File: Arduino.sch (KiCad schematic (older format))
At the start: 20 parts

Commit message: Arduino layout
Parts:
- added R13, R14, R55: R, symbol R
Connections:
- net GND: now also R14.2, R55.2
- net at ARD1.1 (5V): now also R13.1
- net at ARD1.2 (GND): now also R14.1
- net at ARD1.3 (GND): now also R55.1
- new net +5V: R13.2
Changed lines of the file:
@@
 	7900 5200 7900 5600
 $Comp
-L GND #PWR67
+L GND #PWR057
 U 1 1 52FC2D3A
 P 7900 5600
-F 0 "#PWR67" H 7900 5600 30  0001 C CNN
+F 0 "#PWR057" H 7900 5600 30  0001 C CNN
 F 1 "GND" H 7900 5530 30  0001 C CNN
 F 2 "" H 7900 5600 60  0000 C CNN
@@
 $EndComp
 Wire Wire Line
-	2700 4000 2300 4000
+	2700 4000 2000 4000
 Wire Wire Line
 	3200 4000 3750 4000
 $Comp
-L +12P #PWR66
+L +12P #PWR058
 U 1 1 52FC23FA
-P 2300 3800
-F 0 "#PWR66" H 2300 3770 30  0001 C CNN
-F 1 "+12P" H 2300 3900 30  0000 C CNN
-F 2 "" H 2300 3800 60  0000 C CNN
-F 3 "" H 2300 3800 60  0000 C CNN
-	1    2300 3800
+P 2000 3800
+F 0 "#PWR058" H 2000 3770 30  0001 C CNN
+F 1 "+12P" H 2000 3900 30  0000 C CNN
+F 2 "" H 2000 3800 60  0000 C CNN
+F 3 "" H 2000 3800 60  0000 C CNN
+	1    2000 3800
 	1    0    0    -1
 $EndComp
 Wire Wire Line
-	2300 4000 2300 3800
+	2000 4000 2000 3800
 Text HLabel 7100 4400 2    60   Output ~ 0
 ~RESET
@@
 Wire Wire Line
 	5650 5000 6200 5000
+$Comp
+L R R13
+U 1 1 531F5FF6
+P 2950 3400
+F 0 "R13" V 3030 3400 40  0000 C CNN
+F 1 "R" V 2957 3401 40  0000 C CNN
+F 2 "" V 2880 3400 30  0000 C CNN
+F 3 "" H 2950 3400 30  0000 C CNN
+	1    2950 3400
+	0    1    -1   0
+$EndComp
+Wire Wire Line
+	2700 3400 2000 3400
+Wire Wire Line
+	3200 3400 3750 3400
+Wire Wire Line
+	2000 3400 2000 3200
+$Comp
+L +5V #PWR059
+U 1 1 531F6007
+P 2000 3200
+F 0 "#PWR059" H 2000 3290 20  0001 C CNN
+F 1 "+5V" H 2000 3290 30  0000 C CNN
+F 2 "" H 2000 3200 60  0000 C CNN
+F 3 "" H 2000 3200 60  0000 C CNN
+	1    2000 3200
+	1    0    0    -1
+$EndComp
+$Comp
+L R R14
+U 1 1 531F6023
+P 2950 3600
+F 0 "R14" V 3030 3600 40  0000 C CNN
+F 1 "R" V 2957 3601 40  0000 C CNN
+F 2 "" V 2880 3600 30  0000 C CNN
+F 3 "" H 2950 3600 30  0000 C CNN
+	1    2950 3600
+	0    1    -1   0
+$EndComp
+Wire Wire Line
+	3200 3600 3750 3600
+$Comp
+L R R55
+U 1 1 531F602A
+P 2950 3800
+F 0 "R55" V 3030 3800 40  0000 C CNN
+F 1 "R" V 2957 3801 40  0000 C CNN
+F 2 "" V 2880 3800 30  0000 C CNN
+F 3 "" H 2950 3800 30  0000 C CNN
+	1    2950 3800
+	0    1    -1   0
+$EndComp
+Wire Wire Line
+	3200 3800 3750 3800
+Wire Wire Line
+	2250 3600 2250 3800
+$Comp
+L GND #PWR060
+U 1 1 531F6032
+P 2250 3800
+F 0 "#PWR060" H 2250 3800 30  0001 C CNN
+F 1 "GND" H 2250 3730 30  0001 C CNN
+F 2 "" H 2250 3800 60  0000 C CNN
+F 3 "" H 2250 3800 60  0000 C CNN
+	1    2250 3800
+	1    0    0    -1
+$EndComp
+Wire Wire Line
+	2250 3600 2700 3600
+Wire Wire Line
+	2700 3800 2500 3800
+Wire Wire Line
+	2500 3800 2500 3600
+Connection ~ 2500 3600
 $EndSCHEMATC

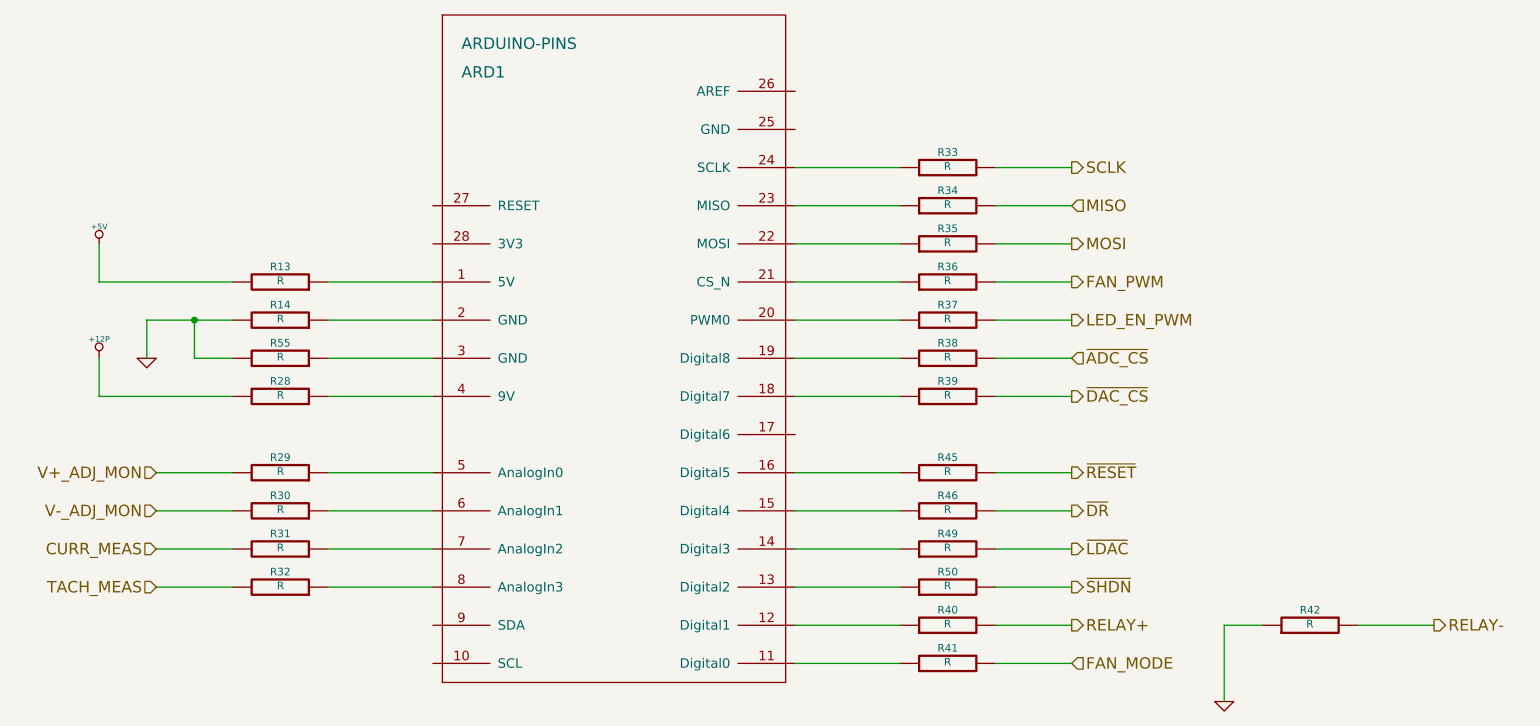
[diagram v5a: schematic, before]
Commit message: Assigned values to passives in Arduino, power adjustment monitor, relay and terminal block schematics
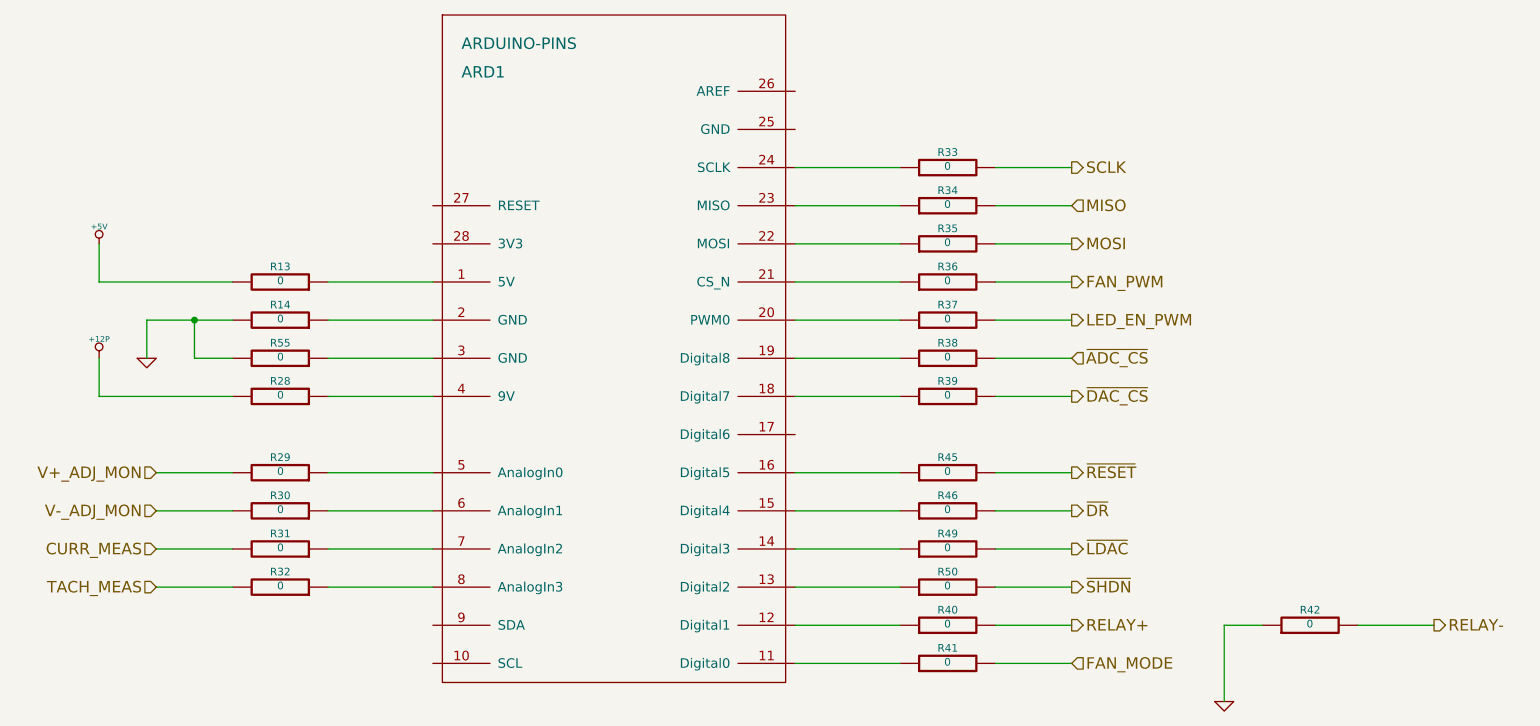
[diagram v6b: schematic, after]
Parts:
- R13, R14, R28, R29, R30, R31, R32, R33, R34, R35, R36, R37, R38, R39, R40, R41, R42, R45, R46, R49, R50, R55: value R -> 0
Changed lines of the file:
@@
 P 6450 3400
 F 0 "R36" V 6530 3400 40  0000 C CNN
-F 1 "R" V 6457 3401 40  0000 C CNN
+F 1 "0" V 6457 3401 40  0000 C CNN
 F 2 "" V 6380 3400 30  0000 C CNN
 F 3 "" H 6450 3400 30  0000 C CNN
@@
 P 6450 5200
 F 0 "R40" V 6530 5200 40  0000 C CNN
-F 1 "R" V 6457 5201 40  0000 C CNN
+F 1 "0" V 6457 5201 40  0000 C CNN
 F 2 "" V 6380 5200 30  0000 C CNN
 F 3 "" H 6450 5200 30  0000 C CNN
@@
 P 2950 5000
 F 0 "R32" V 3030 5000 40  0000 C CNN
-F 1 "R" V 2957 5001 40  0000 C CNN
+F 1 "0" V 2957 5001 40  0000 C CNN
 F 2 "" V 2880 5000 30  0000 C CNN
 F 3 "" H 2950 5000 30  0000 C CNN
@@
 P 2950 4800
 F 0 "R31" V 3030 4800 40  0000 C CNN
-F 1 "R" V 2957 4801 40  0000 C CNN
+F 1 "0" V 2957 4801 40  0000 C CNN
 F 2 "" V 2880 4800 30  0000 C CNN
 F 3 "" H 2950 4800 30  0000 C CNN
@@
 P 2950 4600
 F 0 "R30" V 3030 4600 40  0000 C CNN
-F 1 "R" V 2957 4601 40  0000 C CNN
+F 1 "0" V 2957 4601 40  0000 C CNN
 F 2 "" V 2880 4600 30  0000 C CNN
 F 3 "" H 2950 4600 30  0000 C CNN
@@
 P 2950 4400
 F 0 "R29" V 3030 4400 40  0000 C CNN
-F 1 "R" V 2957 4401 40  0000 C CNN
+F 1 "0" V 2957 4401 40  0000 C CNN
 F 2 "" V 2880 4400 30  0000 C CNN
 F 3 "" H 2950 4400 30  0000 C CNN
@@
 P 6450 3000
 F 0 "R34" V 6530 3000 40  0000 C CNN
-F 1 "R" V 6457 3001 40  0000 C CNN
+F 1 "0" V 6457 3001 40  0000 C CNN
 F 2 "" V 6380 3000 30  0000 C CNN
 F 3 "" H 6450 3000 30  0000 C CNN
@@
 P 6450 2800
 F 0 "R33" V 6530 2800 40  0000 C CNN
-F 1 "R" V 6457 2801 40  0000 C CNN
+F 1 "0" V 6457 2801 40  0000 C CNN
 F 2 "" V 6380 2800 30  0000 C CNN
 F 3 "" H 6450 2800 30  0000 C CNN
@@
 P 6450 4000
 F 0 "R39" V 6530 4000 40  0000 C CNN
-F 1 "R" V 6457 4001 40  0000 C CNN
+F 1 "0" V 6457 4001 40  0000 C CNN
 F 2 "" V 6380 4000 30  0000 C CNN
 F 3 "" H 6450 4000 30  0000 C CNN
@@
 P 6450 3200
 F 0 "R35" V 6530 3200 40  0000 C CNN
-F 1 "R" V 6457 3201 40  0000 C CNN
+F 1 "0" V 6457 3201 40  0000 C CNN
 F 2 "" V 6380 3200 30  0000 C CNN
 F 3 "" H 6450 3200 30  0000 C CNN
@@
 P 8350 5200
 F 0 "R42" V 8430 5200 40  0000 C CNN
-F 1 "R" V 8357 5201 40  0000 C CNN
+F 1 "0" V 8357 5201 40  0000 C CNN
 F 2 "" V 8280 5200 30  0000 C CNN
 F 3 "" H 8350 5200 30  0000 C CNN
@@
 P 6450 3600
 F 0 "R37" V 6530 3600 40  0000 C CNN
-F 1 "R" V 6457 3601 40  0000 C CNN
+F 1 "0" V 6457 3601 40  0000 C CNN
 F 2 "" V 6380 3600 30  0000 C CNN
 F 3 "" H 6450 3600 30  0000 C CNN
@@
 P 6450 3800
 F 0 "R38" V 6530 3800 40  0000 C CNN
-F 1 "R" V 6457 3801 40  0000 C CNN
+F 1 "0" V 6457 3801 40  0000 C CNN
 F 2 "" V 6380 3800 30  0000 C CNN
 F 3 "" H 6450 3800 30  0000 C CNN
@@
 P 6450 5400
 F 0 "R41" V 6530 5400 40  0000 C CNN
-F 1 "R" V 6457 5401 40  0000 C CNN
+F 1 "0" V 6457 5401 40  0000 C CNN
 F 2 "" V 6380 5400 30  0000 C CNN
 F 3 "" H 6450 5400 30  0000 C CNN
@@
 P 2950 4000
 F 0 "R28" V 3030 4000 40  0000 C CNN
-F 1 "R" V 2957 4001 40  0000 C CNN
+F 1 "0" V 2957 4001 40  0000 C CNN
 F 2 "" V 2880 4000 30  0000 C CNN
 F 3 "" H 2950 4000 30  0000 C CNN
@@
 P 6450 4400
 F 0 "R45" V 6530 4400 40  0000 C CNN
-F 1 "R" V 6457 4401 40  0000 C CNN
+F 1 "0" V 6457 4401 40  0000 C CNN
 F 2 "" V 6380 4400 30  0000 C CNN
 F 3 "" H 6450 4400 30  0000 C CNN
@@
 P 6450 4600
 F 0 "R46" V 6530 4600 40  0000 C CNN
-F 1 "R" V 6457 4601 40  0000 C CNN
+F 1 "0" V 6457 4601 40  0000 C CNN
 F 2 "" V 6380 4600 30  0000 C CNN
 F 3 "" H 6450 4600 30  0000 C CNN
@@
 P 6450 4800
 F 0 "R49" V 6530 4800 40  0000 C CNN
-F 1 "R" V 6457 4801 40  0000 C CNN
+F 1 "0" V 6457 4801 40  0000 C CNN
 F 2 "" V 6380 4800 30  0000 C CNN
 F 3 "" H 6450 4800 30  0000 C CNN
@@
 P 6450 5000
 F 0 "R50" V 6530 5000 40  0000 C CNN
-F 1 "R" V 6457 5001 40  0000 C CNN
+F 1 "0" V 6457 5001 40  0000 C CNN
 F 2 "" V 6380 5000 30  0000 C CNN
 F 3 "" H 6450 5000 30  0000 C CNN
@@
 P 2950 3400
 F 0 "R13" V 3030 3400 40  0000 C CNN
-F 1 "R" V 2957 3401 40  0000 C CNN
+F 1 "0" V 2957 3401 40  0000 C CNN
 F 2 "" V 2880 3400 30  0000 C CNN
 F 3 "" H 2950 3400 30  0000 C CNN
@@
 P 2950 3600
 F 0 "R14" V 3030 3600 40  0000 C CNN
-F 1 "R" V 2957 3601 40  0000 C CNN
+F 1 "0" V 2957 3601 40  0000 C CNN
 F 2 "" V 2880 3600 30  0000 C CNN
 F 3 "" H 2950 3600 30  0000 C CNN
@@
 P 2950 3800
 F 0 "R55" V 3030 3800 40  0000 C CNN
-F 1 "R" V 2957 3801 40  0000 C CNN
+F 1 "0" V 2957 3801 40  0000 C CNN
 F 2 "" V 2880 3800 30  0000 C CNN
 F 3 "" H 2950 3800 30  0000 C CNN

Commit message: Back-annotated footprints into the schematic
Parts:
- ARD1: footprint (none) -> BenchBudEE:Arduino
- R13, R14, R28, R29, R30, R31, R32, R33, R34, R35, R36, R37, R38, R39, R40, R41, R42, R45, R46, R49, R50, R55: footprint (none) -> BenchBudEE:Resistor_SMD0805_Blob
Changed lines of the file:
@@
 F 0 "ARD1" H 3900 5900 60  0000 L CNN
 F 1 "ARDUINO-PINS" H 3900 6050 60  0000 L CNN
-F 2 "" H 4700 4100 60  0000 C CNN
+F 2 "BenchBudEE:Arduino" H 4700 4100 60  0001 C CNN
 F 3 "" H 4700 4100 60  0000 C CNN
 	1    4700 4100
@@
 F 0 "R36" V 6530 3400 40  0000 C CNN
 F 1 "0" V 6457 3401 40  0000 C CNN
-F 2 "" V 6380 3400 30  0000 C CNN
+F 2 "BenchBudEE:Resistor_SMD0805_Blob" V 6380 3400 30  0001 C CNN
 F 3 "" H 6450 3400 30  0000 C CNN
 	1    6450 3400
@@
 F 0 "R40" V 6530 5200 40  0000 C CNN
 F 1 "0" V 6457 5201 40  0000 C CNN
-F 2 "" V 6380 5200 30  0000 C CNN
+F 2 "BenchBudEE:Resistor_SMD0805_Blob" V 6380 5200 30  0001 C CNN
 F 3 "" H 6450 5200 30  0000 C CNN
 	1    6450 5200
@@
 	7900 5200 7900 5600
 $Comp
-L GND #PWR061
+L GND #PWR060
 U 1 1 52FC2D3A
 P 7900 5600
-F 0 "#PWR061" H 7900 5600 30  0001 C CNN
+F 0 "#PWR060" H 7900 5600 30  0001 C CNN
 F 1 "GND" H 7900 5530 30  0001 C CNN
 F 2 "" H 7900 5600 60  0000 C CNN
@@
 F 0 "R32" V 3030 5000 40  0000 C CNN
 F 1 "0" V 2957 5001 40  0000 C CNN
-F 2 "" V 2880 5000 30  0000 C CNN
+F 2 "BenchBudEE:Resistor_SMD0805_Blob" V 2880 5000 30  0001 C CNN
 F 3 "" H 2950 5000 30  0000 C CNN
 	1    2950 5000
@@
 F 0 "R31" V 3030 4800 40  0000 C CNN
 F 1 "0" V 2957 4801 40  0000 C CNN
-F 2 "" V 2880 4800 30  0000 C CNN
+F 2 "BenchBudEE:Resistor_SMD0805_Blob" V 2880 4800 30  0001 C CNN
 F 3 "" H 2950 4800 30  0000 C CNN
 	1    2950 4800
@@
 F 0 "R30" V 3030 4600 40  0000 C CNN
 F 1 "0" V 2957 4601 40  0000 C CNN
-F 2 "" V 2880 4600 30  0000 C CNN
+F 2 "BenchBudEE:Resistor_SMD0805_Blob" V 2880 4600 30  0001 C CNN
 F 3 "" H 2950 4600 30  0000 C CNN
 	1    2950 4600
@@
 F 0 "R29" V 3030 4400 40  0000 C CNN
 F 1 "0" V 2957 4401 40  0000 C CNN
-F 2 "" V 2880 4400 30  0000 C CNN
+F 2 "BenchBudEE:Resistor_SMD0805_Blob" V 2880 4400 30  0001 C CNN
 F 3 "" H 2950 4400 30  0000 C CNN
 	1    2950 4400
@@
 F 0 "R34" V 6530 3000 40  0000 C CNN
 F 1 "0" V 6457 3001 40  0000 C CNN
-F 2 "" V 6380 3000 30  0000 C CNN
+F 2 "BenchBudEE:Resistor_SMD0805_Blob" V 6380 3000 30  0001 C CNN
 F 3 "" H 6450 3000 30  0000 C CNN
 	1    6450 3000
@@
 F 0 "R33" V 6530 2800 40  0000 C CNN
 F 1 "0" V 6457 2801 40  0000 C CNN
-F 2 "" V 6380 2800 30  0000 C CNN
+F 2 "BenchBudEE:Resistor_SMD0805_Blob" V 6380 2800 30  0001 C CNN
 F 3 "" H 6450 2800 30  0000 C CNN
 	1    6450 2800
@@
 F 0 "R39" V 6530 4000 40  0000 C CNN
 F 1 "0" V 6457 4001 40  0000 C CNN
-F 2 "" V 6380 4000 30  0000 C CNN
+F 2 "BenchBudEE:Resistor_SMD0805_Blob" V 6380 4000 30  0001 C CNN
 F 3 "" H 6450 4000 30  0000 C CNN
 	1    6450 4000
@@
 F 0 "R35" V 6530 3200 40  0000 C CNN
 F 1 "0" V 6457 3201 40  0000 C CNN
-F 2 "" V 6380 3200 30  0000 C CNN
+F 2 "BenchBudEE:Resistor_SMD0805_Blob" V 6380 3200 30  0001 C CNN
 F 3 "" H 6450 3200 30  0000 C CNN
 	1    6450 3200
@@
 F 0 "R42" V 8430 5200 40  0000 C CNN
 F 1 "0" V 8357 5201 40  0000 C CNN
-F 2 "" V 8280 5200 30  0000 C CNN
+F 2 "BenchBudEE:Resistor_SMD0805_Blob" V 8280 5200 30  0001 C CNN
 F 3 "" H 8350 5200 30  0000 C CNN
 	1    8350 5200
@@
 F 0 "R37" V 6530 3600 40  0000 C CNN
 F 1 "0" V 6457 3601 40  0000 C CNN
-F 2 "" V 6380 3600 30  0000 C CNN
+F 2 "BenchBudEE:Resistor_SMD0805_Blob" V 6380 3600 30  0001 C CNN
 F 3 "" H 6450 3600 30  0000 C CNN
 	1    6450 3600
@@
 F 0 "R38" V 6530 3800 40  0000 C CNN
 F 1 "0" V 6457 3801 40  0000 C CNN
-F 2 "" V 6380 3800 30  0000 C CNN
+F 2 "BenchBudEE:Resistor_SMD0805_Blob" V 6380 3800 30  0001 C CNN
 F 3 "" H 6450 3800 30  0000 C CNN
 	1    6450 3800
@@
 F 0 "R41" V 6530 5400 40  0000 C CNN
 F 1 "0" V 6457 5401 40  0000 C CNN
-F 2 "" V 6380 5400 30  0000 C CNN
+F 2 "BenchBudEE:Resistor_SMD0805_Blob" V 6380 5400 30  0001 C CNN
 F 3 "" H 6450 5400 30  0000 C CNN
 	1    6450 5400
@@
 F 0 "R28" V 3030 4000 40  0000 C CNN
 F 1 "0" V 2957 4001 40  0000 C CNN
-F 2 "" V 2880 4000 30  0000 C CNN
+F 2 "BenchBudEE:Resistor_SMD0805_Blob" V 2880 4000 30  0001 C CNN
 F 3 "" H 2950 4000 30  0000 C CNN
 	1    2950 4000
@@
 	3200 4000 3750 4000
 $Comp
-L +12P #PWR062
+L +12P #PWR061
 U 1 1 52FC23FA
 P 2000 3800
-F 0 "#PWR062" H 2000 3770 30  0001 C CNN
+F 0 "#PWR061" H 2000 3770 30  0001 C CNN
 F 1 "+12P" H 2000 3900 30  0000 C CNN
 F 2 "" H 2000 3800 60  0000 C CNN
@@
 F 0 "R45" V 6530 4400 40  0000 C CNN
 F 1 "0" V 6457 4401 40  0000 C CNN
-F 2 "" V 6380 4400 30  0000 C CNN
+F 2 "BenchBudEE:Resistor_SMD0805_Blob" V 6380 4400 30  0001 C CNN
 F 3 "" H 6450 4400 30  0000 C CNN
 	1    6450 4400
@@
 F 0 "R46" V 6530 4600 40  0000 C CNN
 F 1 "0" V 6457 4601 40  0000 C CNN
-F 2 "" V 6380 4600 30  0000 C CNN
+F 2 "BenchBudEE:Resistor_SMD0805_Blob" V 6380 4600 30  0001 C CNN
 F 3 "" H 6450 4600 30  0000 C CNN
 	1    6450 4600
@@
 F 0 "R49" V 6530 4800 40  0000 C CNN
 F 1 "0" V 6457 4801 40  0000 C CNN
-F 2 "" V 6380 4800 30  0000 C CNN
+F 2 "BenchBudEE:Resistor_SMD0805_Blob" V 6380 4800 30  0001 C CNN
 F 3 "" H 6450 4800 30  0000 C CNN
 	1    6450 4800
@@
 F 0 "R50" V 6530 5000 40  0000 C CNN
 F 1 "0" V 6457 5001 40  0000 C CNN
-F 2 "" V 6380 5000 30  0000 C CNN
+F 2 "BenchBudEE:Resistor_SMD0805_Blob" V 6380 5000 30  0001 C CNN
 F 3 "" H 6450 5000 30  0000 C CNN
 	1    6450 5000
@@
 F 0 "R13" V 3030 3400 40  0000 C CNN
 F 1 "0" V 2957 3401 40  0000 C CNN
-F 2 "" V 2880 3400 30  0000 C CNN
+F 2 "BenchBudEE:Resistor_SMD0805_Blob" V 2880 3400 30  0001 C CNN
 F 3 "" H 2950 3400 30  0000 C CNN
 	1    2950 3400
@@
 	2000 3400 2000 3200
 $Comp
-L +5V #PWR063
+L +5V #PWR062
 U 1 1 531F6007
 P 2000 3200
-F 0 "#PWR063" H 2000 3290 20  0001 C CNN
+F 0 "#PWR062" H 2000 3290 20  0001 C CNN
 F 1 "+5V" H 2000 3290 30  0000 C CNN
 F 2 "" H 2000 3200 60  0000 C CNN
@@
 F 0 "R14" V 3030 3600 40  0000 C CNN
 F 1 "0" V 2957 3601 40  0000 C CNN
-F 2 "" V 2880 3600 30  0000 C CNN
+F 2 "BenchBudEE:Resistor_SMD0805_Blob" V 2880 3600 30  0001 C CNN
 F 3 "" H 2950 3600 30  0000 C CNN
 	1    2950 3600
@@
 F 0 "R55" V 3030 3800 40  0000 C CNN
 F 1 "0" V 2957 3801 40  0000 C CNN
-F 2 "" V 2880 3800 30  0000 C CNN
+F 2 "BenchBudEE:Resistor_SMD0805_Blob" V 2880 3800 30  0001 C CNN
 F 3 "" H 2950 3800 30  0000 C CNN
 	1    2950 3800
@@
 	2250 3600 2250 3800
 $Comp
-L GND #PWR064
+L GND #PWR063
 U 1 1 531F6032
 P 2250 3800
-F 0 "#PWR064" H 2250 3800 30  0001 C CNN
+F 0 "#PWR063" H 2250 3800 30  0001 C CNN
 F 1 "GND" H 2250 3730 30  0001 C CNN
 F 2 "" H 2250 3800 60  0000 C CNN

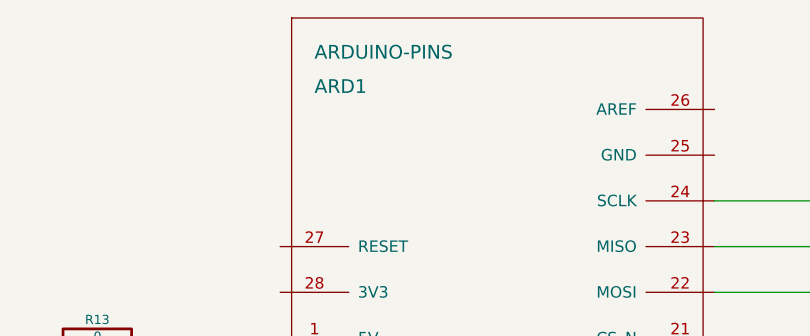
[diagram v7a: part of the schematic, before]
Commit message: Final part numbers added to schematic, cross-checked KiCAD BOM against manual BOM
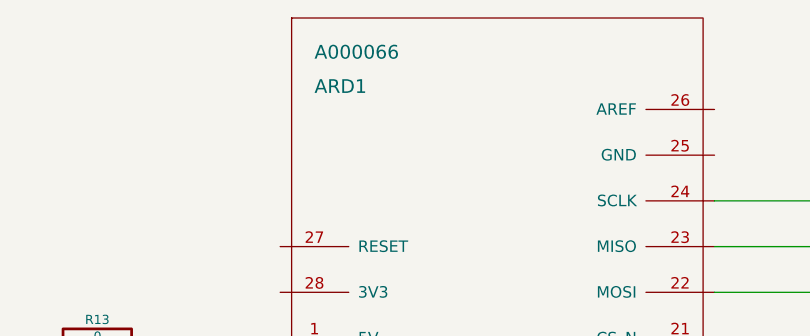
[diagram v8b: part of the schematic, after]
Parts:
- ARD1: value ARDUINO-PINS -> A000066
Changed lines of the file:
@@
 P 4700 4100
 F 0 "ARD1" H 3900 5900 60  0000 L CNN
-F 1 "ARDUINO-PINS" H 3900 6050 60  0000 L CNN
+F 1 "A000066" H 3900 6050 60  0000 L CNN
 F 2 "BenchBudEE:Arduino" H 4700 4100 60  0001 C CNN
 F 3 "" H 4700 4100 60  0000 C CNN
